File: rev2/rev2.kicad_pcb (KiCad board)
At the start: 4 copper layers, 49.9 x 49.8 mm, 54 parts, among them J1 Termination, J10 GPIO, J2 CAN1, J3 Termination, J4 CAN2, J5 SWD ASYNC, J6 LIN Pots, J7 AIN, J8 USB_OTG, J9 PWR_USB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

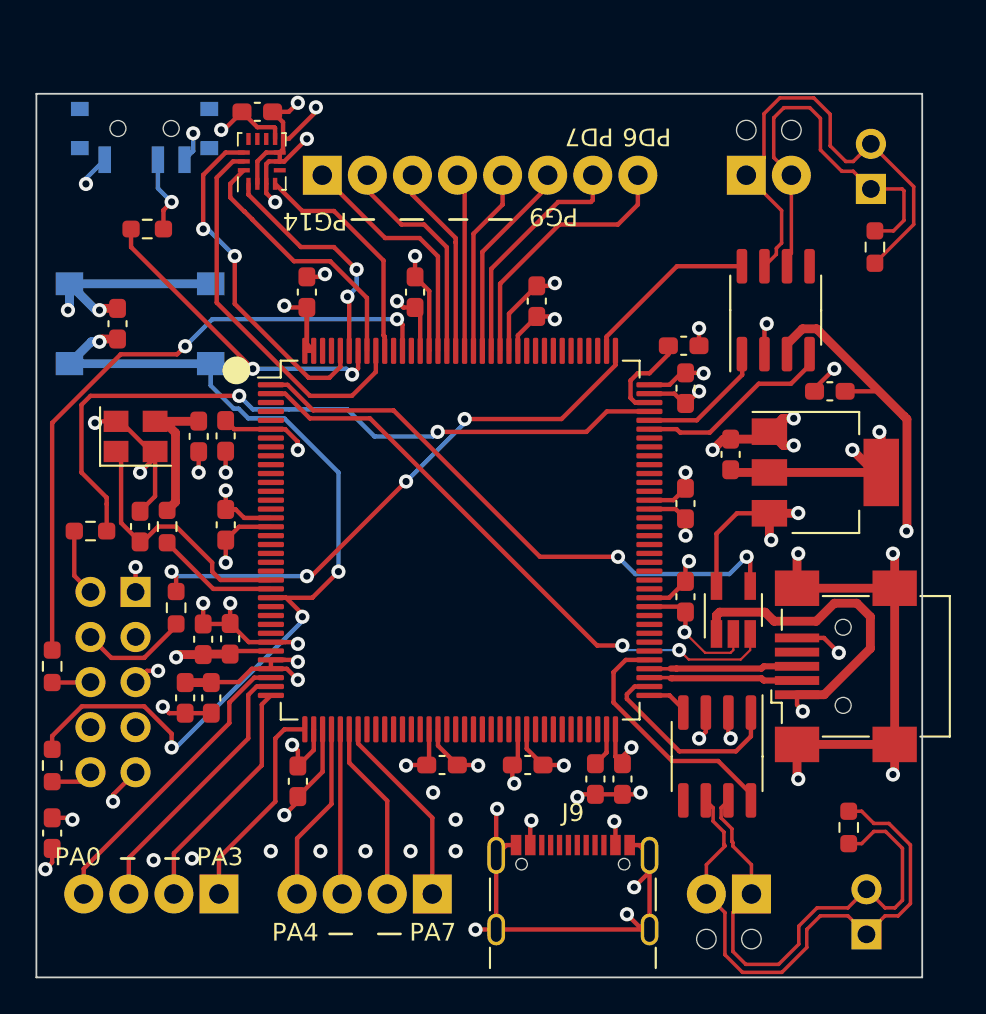
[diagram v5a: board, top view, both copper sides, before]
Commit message: tweaked the differential traces and made thhem compliant to JLC04161H-7628 guidlines for controlled impedance. Also I think I might remove the 10 pin header for SWD/JTAG in favor of just SWD to safe on space.
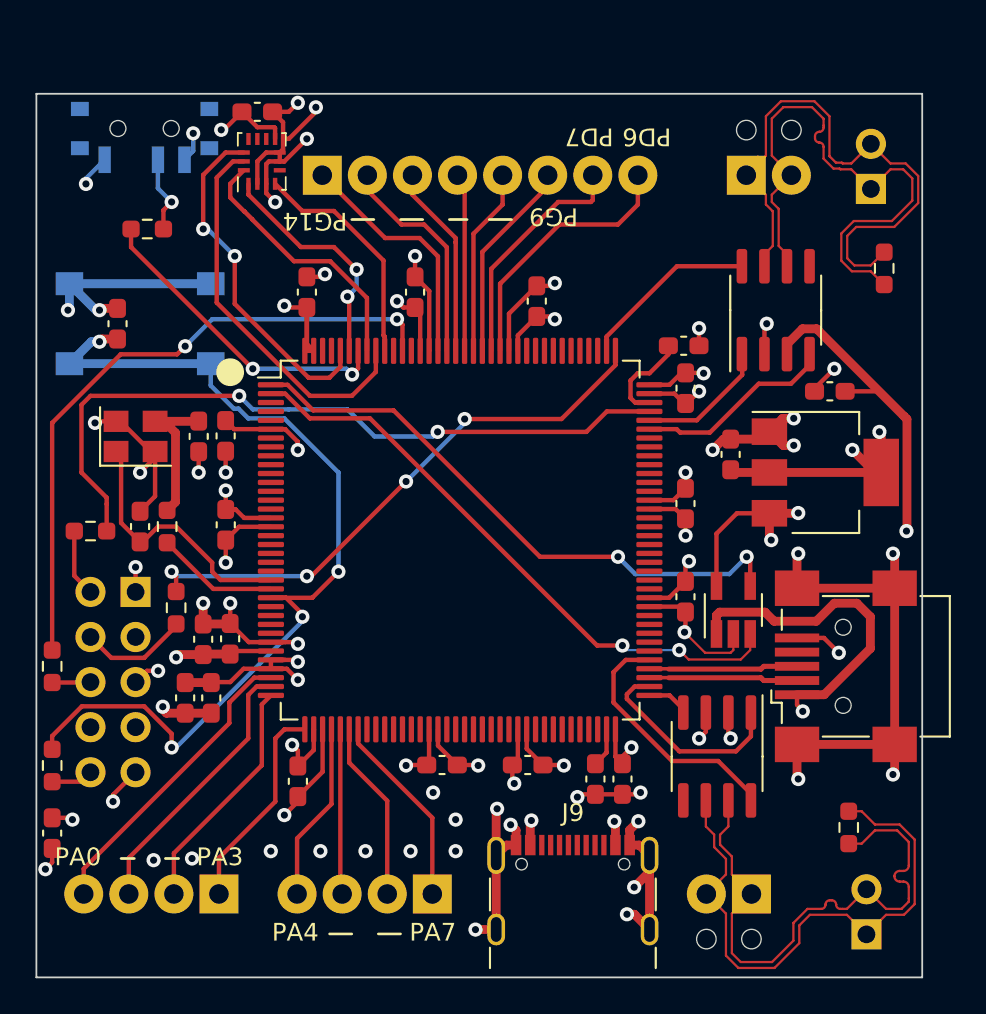
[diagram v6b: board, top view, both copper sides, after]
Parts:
- moved R4 1.31 mm to (157.8, 83.8), turned to 90 degrees
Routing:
- net /CAN1-: track 23.0 -> 33.5 mm
- net /CAN1+: track 28.2 -> 34.0 mm
- net GND: track 167.6 -> 161.9 mm, vias 53 -> 55
- net /CAN2+: track 29.8 -> 32.5 mm
- net /CAN2-: track 31.5 -> 32.1 mm
- added copper zone on In2.Cu, net +3.3V
- added copper zone on In2.Cu, net +5V
- added copper zone on In1.Cu, net GND
- removed copper zone on In1.Cu, net +3.3V
- removed copper zone on In1.Cu, net +5V
- removed copper zone on In2.Cu, net GND

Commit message: removed the 10 pin SWD/JTAG header in favor of just a 3 pin SWD connector.in addition, also added a 3.3V and a 5V header for external power supplies
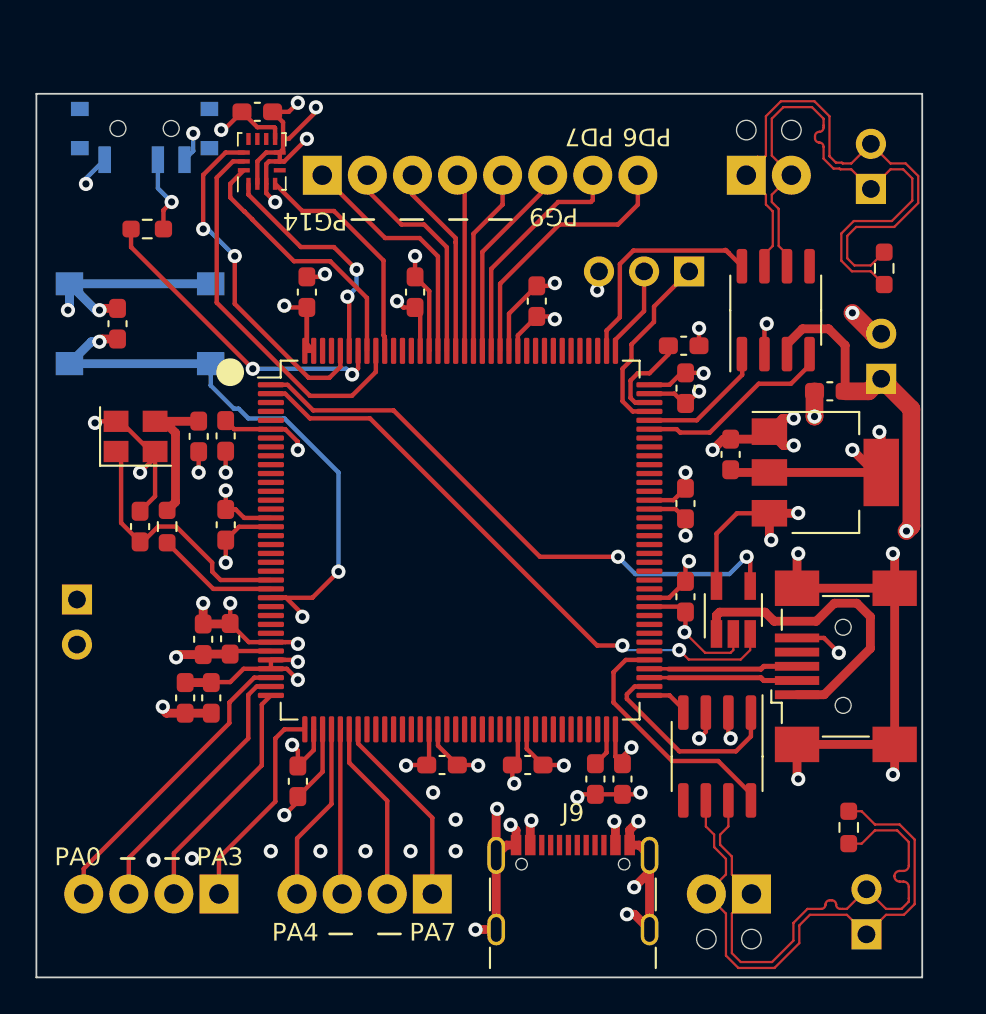
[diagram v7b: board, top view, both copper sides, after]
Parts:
- removed C25: 500n, Capacitor_SMD:C_0603_1608Metric_Pad1.08x0.95mm_HandSolder
- removed R2, R6, R7, R8: 100, Resistor_SMD:R_0603_1608Metric_Pad0.98x0.95mm_HandSolder
- added J11: SWD, Connector_PinHeader_2.54mm:PinHeader_1x03_P2.54mm_Vertical, B.Cu at (146.8, 83.9)
- added J12: 5V power breakout, Connector_PinHeader_2.54mm:PinHeader_1x02_P2.54mm_Vertical, B.Cu at (157.6, 90.0)
- J5: value SWD ASYNC -> 3.3V power breakout; footprint Connector_PinHeader_2.54mm:PinHeader_2x05_P2.54mm_Vertical -> Connector_PinHeader_2.54mm:PinHeader_1x02_P2.54mm_Vertical
- moved G*** 5.00 mm to (153.7, 98.2)
- moved J5 3.33 mm to (112.3, 102.4)
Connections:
- J5 pad 2: Net-(J5-Pin_2) -> GND
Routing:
- net SYS_JTDO_SWO: track 36.6 -> 0.00 mm, vias 2 -> 0
- net SYS_JTMS_SWDIO: track 41.4 -> 10.6 mm, vias 2 -> 0
- net SYS_JTCK_SWCLK: track 32.2 -> 5.14 mm, vias 4 -> 0
- net NRST: track 54.2 -> 34.3 mm, vias 4 -> 3
- net Net-(J5-Pin_4): track 6.17 -> 0.00 mm
- net Net-(J5-Pin_2): track 3.81 -> 0.00 mm
- net /Silent Mode 1: track 10.1 -> 13.0 mm
- net +3.3V: track 91.4 -> 88.8 mm, vias 23 -> 21
- net Net-(J5-Pin_10): track 2.38 -> 0.00 mm
- net Net-(J5-Pin_6): track 2.17 -> 0.00 mm
- net GND: track 161.9 -> 159.9 mm, vias 55 -> 54
- net +5V: track 34.6 -> 33.5 mm
- net /VBUS1: track 18.5 -> 17.7 mm, vias 1 -> 0
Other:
- board text removed: "2"
